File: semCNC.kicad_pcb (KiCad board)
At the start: 2 copper layers, 134 parts, among them P1 CONN_01X04, P10 CONN_01X05, P11 CONN_01X03, P12 CONN_02X08, P13 CONN_01X05, P14 CONN_01X03, P15 CONN_02X08, P16 CONN_01X05, P17 CONN_01X03, P18 CONN_02X08, P19 POWER_HEAD, P2 LPT port, P3 CONN_01X04, P4 EXPANDER PAD, P5 CONN_01X02, P6 CONN_01X02, P7 CONN_01X05, P8 CONN_01X03, P9 CONN_02X08, T1 TRANSFO, U1 MSP430G2452, U2 TIdac08s085, U3 LD1117S33CTR, U4 SPX2920U-3.3, U5 DRV8825, U6 DRV8825, U7 DRV8825, U8 DRV8825

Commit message: mer elegem van .... :P
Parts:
- added P20: CONN_01X02, Pin_Headers:Pin_Header_Straight_1x02, F.Cu at (587.6, 98.4)
- C12, C7, C8, C9: moved to B.Cu
- moved R14 146.3 mm to (351.4, 95.4), turned to 180 degrees
- moved R9 141.1 mm to (367.4, 140.1)
- moved R5 134.7 mm to (367.4, 148.7)
- moved R10 134.4 mm to (367.4, 144.4), turned to 180 degrees
- moved R17 126.8 mm to (375.6, 176.1)
- moved P6 120.0 mm to (602.1, 114.9)
- moved R13 106.3 mm to (383.7, 157.1), turned to 180 degrees
- moved P19 104.6 mm to (529.5, 104.2), turned to 90 degrees
- moved R6 99.1 mm to (399.4, 89.7), turned to 90 degrees
- moved C5 83.1 mm to (560.5, 115.1), turned to 270 degrees
- moved C6 81.4 mm to (579.3, 114.8), turned to 270 degrees
- moved C3 78.1 mm to (462.2, 81.1)
- moved C4 69.4 mm to (447.7, 81.1)
- moved R11 69.2 mm to (457.1, 105.5)
- moved R3 63.5 mm to (521.9, 100.2)
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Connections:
- C14 pad 2: GND -> VMOT_GND
- C15 pad 1: GND -> VMOT_GND
- C19 pad 2: GND -> VMOT_GND
- C20 pad 1: GND -> VMOT_GND
- C24 pad 2: GND -> VMOT_GND
- C25 pad 1: GND -> VMOT_GND
- C29 pad 2: GND -> VMOT_GND
- C30 pad 1: GND -> VMOT_GND
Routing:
- net VMOT_GND: track 9.77 -> 507.7 mm, vias 2 -> 4
- net VMOT: track 226.2 -> 508.6 mm, vias 0 -> 2
- net Net-(P2-Pad2): track 95.4 -> 5.17 mm, vias 1 -> 0
- net 3.3V: track 669.4 -> 742.8 mm, vias 3 -> 4
- net GND: track 48.4 -> 87.9 mm
- net /DRIVER3/STEP: track 34.2 -> 57.9 mm
- net Net-(P5-Pad1): track 24.6 -> 42.4 mm
- net Net-(P5-Pad2): track 22.1 -> 39.0 mm
- net /DRIVER2/STEP: track 36.8 -> 52.1 mm
- net Net-(D1-Pad4): track 30.8 -> 16.9 mm
- net Net-(D1-Pad2): track 41.4 -> 27.5 mm
- net Net-(P3-Pad3): track 39.7 -> 45.6 mm, vias 0 -> 1
- net /MOSI: track 18.5 -> 24.0 mm, vias 0 -> 2
- net /DRIVER4/DIR: track 23.9 -> 28.6 mm
- net /DRIVER1/DIR: track 52.8 -> 57.4 mm
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
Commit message: kicsit tovabb
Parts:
- moved R14 224.3 mm to (559.7, 178.7)
- moved R12 111.5 mm to (558.0, 170.0)
- moved R11 111.5 mm to (544.2, 175.1)
- moved C1 97.0 mm to (497.2, 175.9)
- moved C3 97.0 mm to (497.2, 171.6)
- moved R6 73.3 mm to (428.4, 157.1)
- moved P19 73.1 mm to (524.6, 177.1)
- moved R15 73.1 mm to (517.3, 182.0)
- moved R16 73.1 mm to (525.9, 182.0)
- moved R3 73.1 mm to (517.1, 173.1)
- moved R4 73.1 mm to (525.7, 173.1)
- moved C7 47.5 mm to (591.4, 101.7)
- moved C5 41.9 mm to (601.4, 106.0), turned to 180 degrees
- moved P20 36.8 mm to (591.4, 135.0)
- moved C6 22.9 mm to (601.2, 121.5), turned to 180 degrees
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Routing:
- net 3.3V: track 742.8 -> 649.1 mm
- net /DRIVER4/STEP: track 25.1 -> 67.5 mm, vias 1 -> 2
- net /DRIVER4/nFAULT: track 32.2 -> 70.3 mm, vias 1 -> 2
- net /DRIVER4/DIR: track 28.6 -> 66.5 mm, vias 1 -> 2
- net /DRIVER4/CURR_REF: track 47.5 -> 83.2 mm, vias 0 -> 1
- net VMOT: track 508.6 -> 541.9 mm, vias 2 -> 4
- net /DRIVER1/CURR_REF: track 74.8 -> 45.4 mm
- net /DRIVER3/CURR_REF: track 71.6 -> 45.1 mm
- net /DRIVER2/CURR_REF: track 78.8 -> 56.3 mm
- net /DRIVER1/DIR: track 57.4 -> 35.6 mm
- net /DRIVER3/nFAULT: track 61.1 -> 39.5 mm
- net /DRIVER1/nFAULT: track 77.7 -> 56.7 mm
- net /DRIVER3/DIR: track 44.0 -> 29.2 mm
- net /DRIVER2/nFAULT: track 56.5 -> 42.4 mm
- net /DRIVER1/STEP: track 57.6 -> 45.2 mm
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
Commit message: New layout
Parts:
- added P21: CONN_01X02, Pin_Headers:Pin_Header_Straight_1x02, F.Cu at (386.0, 159.4)
- R1, R10, R11, R12, R13, R14, R15, R16, R2, R3, R4, R5, R6, R7, R8, R9: moved to B.Cu
- moved P18 309.4 mm to (603.6, 194.2), turned to 180 degrees
- moved RV4 272.7 mm to (579.5, 199.3), turned to 0 degrees
- moved D5 271.9 mm to (587.1, 185.3), turned to 270 degrees
- moved R57 257.2 mm to (580.4, 182.3), turned to 0 degrees
- moved R59 254.9 mm to (580.4, 179.7), turned to 0 degrees
- moved R58 252.8 mm to (580.4, 177.2), turned to 180 degrees
- moved P17 252.6 mm to (569.1, 196.8), turned to 0 degrees
- moved R60 250.7 mm to (580.4, 174.7), turned to 0 degrees
- moved R61 248.4 mm to (580.4, 171.8), turned to 0 degrees
- moved R62 246.2 mm to (580.4, 168.7), turned to 0 degrees
- moved R63 244.4 mm to (580.4, 166.2), turned to 0 degrees
- moved R64 242.7 mm to (580.4, 163.6), turned to 0 degrees
- moved R65 241.1 mm to (580.4, 161.1), turned to 0 degrees
- moved C32 230.0 mm to (566.8, 179.0), turned to 180 degrees
- moved P16 228.4 mm to (552.8, 198.0), turned to 180 degrees
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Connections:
- P2 pad 11: /DRIVER2/nFAULT -> /DRIVER3/nFAULT
- P2 pad 12: /DRIVER3/nFAULT -> /DRIVER2/nFAULT
- P2 pad 18: GND -> Net-(P2-Pad18)
- P2 pad 19: GND -> Net-(P2-Pad18)
- P2 pad 20: GND -> Net-(P2-Pad18)
- P2 pad 21: GND -> Net-(P2-Pad18)
- P2 pad 22: GND -> Net-(P2-Pad18)
- P2 pad 23: GND -> Net-(P2-Pad18)
- P2 pad 24: GND -> Net-(P2-Pad18)
- P2 pad 25: GND -> Net-(P2-Pad18)
- R10 pad 1: /DRIVER3/STEP -> /DRIVER2/STEP
- R11 pad 2: /DRIVER3/DIR -> /DRIVER2/DIR
- R12 pad 1: /DRIVER3/DIR -> /DRIVER2/DIR
- R5 pad 2: /DRIVER2/STEP -> /DRIVER3/STEP
- R6 pad 1: /DRIVER2/STEP -> /DRIVER3/STEP
- R7 pad 2: /DRIVER2/DIR -> /DRIVER3/DIR
- R8 pad 1: /DRIVER2/DIR -> /DRIVER3/DIR
- R9 pad 2: /DRIVER3/STEP -> /DRIVER2/STEP
- U1 pad 11: /DRIVER4/STEP -> /DRIVER1/STEP
- U1 pad 15: /DRIVER1/STEP -> /DRIVER4/STEP
- U2 pad 3: /DRIVER3/CURR_REF -> /DRIVER2/CURR_REF
- U2 pad 4: /DRIVER2/CURR_REF -> /DRIVER3/CURR_REF
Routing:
- net 3.3V: track 649.1 -> 961.2 mm, vias 4 -> 2
- net /DRIVER1/DIR: track 35.6 -> 220.0 mm, vias 1 -> 3
- net /DRIVER1/STEP: track 45.2 -> 222.2 mm, vias 1 -> 3
- net /DRIVER4/STEP: track 67.5 -> 239.6 mm, vias 2 -> 3
- net /DRIVER4/DIR: track 66.5 -> 223.5 mm, vias 2 -> 3
- net /DRIVER4/CURR_REF: track 83.2 -> 239.4 mm
- net /DRIVER1/CURR_REF: track 45.4 -> 198.4 mm, vias 0 -> 1
- net /DRIVER2/STEP: track 43.9 -> 190.6 mm, vias 1 -> 3
- net /DRIVER2/DIR: track 35.7 -> 181.3 mm, vias 1 -> 3
- net /DRIVER3/DIR: track 29.2 -> 158.3 mm, vias 1 -> 3
- net /DRIVER2/CURR_REF: track 56.3 -> 180.3 mm, vias 0 -> 1
- net /DRIVER3/CURR_REF: track 45.1 -> 160.4 mm, vias 0 -> 1
- net /DRIVER3/STEP: track 50.5 -> 162.0 mm, vias 1 -> 3
- net /DRIVER2/nFAULT: track 42.4 -> 92.7 mm
- net /DRIVER3/nFAULT: track 39.5 -> 76.5 mm
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
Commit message: new layout
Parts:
- R21, R22, R23, R24, R25, R26, R27, R28, R29, R45, R46, R47, R48, R49, R50, R51, R52, R53, R57, R58, R59, R60, R61, R62, R63, R64, R65: moved to B.Cu
- moved P15 161.2 mm to (625.0, 95.3), turned to 90 degrees
- moved R45 149.9 mm to (632.5, 75.0), turned to 0 degrees
- moved R50 149.9 mm to (632.5, 90.0), turned to 0 degrees
- moved R47 149.9 mm to (632.5, 77.5), turned to 0 degrees
- moved R51 149.9 mm to (632.5, 92.5), turned to 0 degrees
- moved R46 149.9 mm to (632.5, 80.0), turned to 180 degrees
- moved R52 149.9 mm to (632.5, 95.0), turned to 0 degrees
- moved R48 149.8 mm to (632.5, 82.5), turned to 0 degrees
- moved R53 149.8 mm to (632.5, 97.5), turned to 0 degrees
- moved R49 149.8 mm to (632.5, 85.0), turned to 0 degrees
- moved P6 148.1 mm to (475.2, 57.8), turned to 180 degrees
- moved D4 134.7 mm to (632.5, 67.8), turned to 270 degrees
- moved P16 134.4 mm to (649.8, 105.0), turned to 0 degrees
- moved U7 131.8 mm to (632.2, 89.5)
- moved C27 131.5 mm to (635.0, 77.5)
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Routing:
- net 3.3V: track 961.2 -> 695.0 mm, vias 2 -> 1
- net /DRIVER4/CURR_REF: track 239.4 -> 18.6 mm, vias 1 -> 0
- net /DRIVER4/DIR: track 223.5 -> 5.94 mm, vias 3 -> 1
- net /DRIVER1/CURR_REF: track 198.4 -> 0.00 mm, vias 1 -> 0
- net /DRIVER4/STEP: track 239.6 -> 41.2 mm, vias 3 -> 1
- net /DRIVER1/DIR: track 220.0 -> 28.3 mm, vias 3 -> 1
- net /DRIVER1/STEP: track 222.2 -> 37.7 mm, vias 3 -> 1
- net /DRIVER3/CURR_REF: track 160.4 -> 16.6 mm, vias 1 -> 0
- net VMOT: track 525.7 -> 390.5 mm, vias 4 -> 2
- net /DRIVER3/DIR: track 158.3 -> 26.2 mm, vias 3 -> 1
- net /DRIVER2/CURR_REF: track 180.3 -> 52.4 mm, vias 1 -> 0
- net /DRIVER3/STEP: track 162.0 -> 37.0 mm, vias 3 -> 1
- net /DRIVER2/STEP: track 190.6 -> 76.7 mm
- net /DRIVER2/DIR: track 181.3 -> 67.5 mm
- net VMOT_GND: track 471.9 -> 362.9 mm, vias 4 -> 2
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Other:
- net class Default: clearance 0.254 -> 0.3048; via_dia 1 -> 1.6; via_drill 0.4 -> 0.8
- rule trace_clearance: 0.254 -> 0.3048
- board text added: "A rács 0.25mm-es, de csak a nagyobbakat használod ( hátra zoom ) A drv8825 közepe egy nagy rácspontra kerül, mellé a mikrokapcsoló, szimmetrikusan, a legfelső lábát rácspontra helyezve. 1206-os alkatrészeket mindig középen megfogva kell használni, mindig rácspontra kerül. Viák mindig rácspontra kerülnek, kivéve a kettőt, azok a felére. A mikrokapcsolót a 15-ös lábnál kell megfogni, az kerül rácsp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"

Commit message: layout work
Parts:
- R33, R34, R35, R36, R37, R38, R39, R40, R41: moved to B.Cu
- moved C4 237.3 mm to (691.8, 53.5), turned to 270 degrees
- moved P11 183.3 mm to (650.0, 95.2), turned to 180 degrees
- moved RV2 181.2 mm to (655.0, 93.0), turned to 180 degrees
- moved P10 181.0 mm to (627.7, 92.8), turned to 0 degrees
- moved P12 173.7 mm to (652.5, 67.5), turned to 270 degrees
- moved C19 171.1 mm to (632.5, 85.2), turned to 0 degrees
- moved R31 170.5 mm to (625.0, 75.2)
- moved R32 170.2 mm to (625.0, 80.2)
- moved R30 169.6 mm to (640.0, 65.2), turned to 180 degrees
- moved C20 169.2 mm to (632.5, 67.8), turned to 180 degrees
- moved C21 168.7 mm to (640.0, 70.2)
- moved U6 167.9 mm to (645.3, 73.2)
- moved C22 167.8 mm to (643.2, 85.5)
- moved C18 166.4 mm to (640.0, 67.8), turned to 0 degrees
- moved D3 163.1 mm to (645.0, 92.7)
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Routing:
- net (no net): track 17.4 -> 328.3 mm
- net VMOT: track 390.5 -> 107.5 mm, vias 2 -> 0
- net VMOT_GND: track 362.9 -> 88.6 mm, vias 2 -> 0
- net 3.3V: track 695.0 -> 507.6 mm
- net /DRIVER2/nHOME: track 67.3 -> 0.00 mm, vias 1 -> 0
- net /DRIVER2/MODE2: track 60.7 -> 0.00 mm, vias 1 -> 0
- net /DRIVER2/AOUT1: track 55.7 -> 0.00 mm, vias 1 -> 0
- net /DRIVER2/DIR: track 67.5 -> 14.2 mm, vias 3 -> 1
- net /DRIVER2/CURR_REF: track 52.4 -> 2.11 mm
- net /DRIVER2/MODE1: track 50.1 -> 0.00 mm, vias 1 -> 0
- net /DRIVER2/MODE0: track 45.1 -> 0.00 mm, vias 1 -> 0
- net /DRIVER2/AOUT2: track 45.1 -> 0.00 mm, vias 1 -> 0
- net /DRIVER2/STEP: track 76.7 -> 35.1 mm, vias 3 -> 1
- net Net-(P2-Pad18): track 40.7 -> 0.00 mm
- net /DRIVER2/nFAULT: track 39.9 -> 0.00 mm, vias 1 -> 0
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
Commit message: minor changes in layout
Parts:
- removed C3: C, Capacitors_SMD:C_1206_HandSoldering
- U2: value TIdac08s085 -> ANALOG_DEVICES_AD7304; footprint libs:TI_VSSOP10_DGS -> Housings_SOIC:SOIC-16_7.5x10.3mm_Pitch1.27mm
- moved P10 176.1 mm to (792.3, 30.5), turned to 180 degrees
- moved R32 174.0 mm to (795.0, 43.0), turned to 0 degrees
- moved R31 172.2 mm to (795.0, 48.0), turned to 0 degrees
- moved C19 162.0 mm to (787.5, 38.0), turned to 180 degrees
- moved C4 160.1 mm to (531.8, 45.5), turned to 0 degrees
- moved C20 155.5 mm to (787.5, 55.5), turned to 0 degrees
- moved P4 148.7 mm to (645.0, 107.3), turned to 0 degrees
- moved D3 144.1 mm to (775.0, 30.5), turned to 90 degrees
- moved C22 141.8 mm to (776.8, 37.8), turned to 0 degrees
- moved C21 141.1 mm to (780.0, 53.0), turned to 0 degrees
- moved C18 140.5 mm to (780.0, 55.5), turned to 180 degrees
- moved R30 140.2 mm to (780.0, 58.0), turned to 0 degrees
- moved R33 140.1 mm to (775.0, 35.5), turned to 0 degrees
- moved R35 138.3 mm to (775.0, 38.0), turned to 0 degrees
- moved P11 137.6 mm to (770.0, 28.0), turned to 0 degrees
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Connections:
- C1 pad 1: 3.3V -> GND
- C1 pad 2: GND -> 3.3V
- P10 pad 5: Net-(P10-Pad5) -> (no net)
- P13 pad 5: Net-(P13-Pad5) -> (no net)
- P16 pad 5: Net-(P16-Pad5) -> (no net)
- P7 pad 5: Net-(P7-Pad5) -> (no net)
- U1 pad 5: Net-(U1-Pad5) -> (no net)
- U2 pad 1: 3.3V -> /DRIVER1/CURR_REF
- U2 pad 2: /DRIVER4/CURR_REF -> /DRIVER3/CURR_REF
- U2 pad 3: /DRIVER2/CURR_REF -> (no net)
- U2 pad 4: /DRIVER3/CURR_REF -> 3.3V
- U2 pad 5: /DRIVER1/CURR_REF -> 3.3V
- U2 pad 7: 3.3V -> GND
- U2 pad 8: /MOSI -> 3.3V
- U5 pad 23: Net-(U5-Pad23) -> (no net)
- U6 pad 23: Net-(U6-Pad23) -> (no net)
- U7 pad 23: Net-(U7-Pad23) -> (no net)
- U8 pad 23: Net-(U8-Pad23) -> (no net)
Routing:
- net (no net): track 328.3 -> 122.1 mm
- net 3.3V: track 507.6 -> 613.2 mm
- net VMOT: track 107.5 -> 157.6 mm
- net VMOT_GND: track 88.6 -> 127.4 mm
- net /DRIVER3/AOUT1: track 0.00 -> 37.0 mm, vias 0 -> 1
- net Net-(P2-Pad18): track 0.00 -> 32.3 mm
- net Net-(P14-Pad2): track 0.00 -> 30.9 mm, vias 0 -> 2
- net /DRIVER3/CURR_REF: track 1.54 -> 32.2 mm
- net /PIN11: track 0.00 -> 27.9 mm
- net Net-(P8-Pad2): track 2.69 -> 30.2 mm, vias 0 -> 2
- net /DRIVER3/AOUT2: track 0.00 -> 26.2 mm, vias 0 -> 1
- net /PIN10: track 0.00 -> 25.3 mm
- net GND: track 58.1 -> 82.6 mm
- net /PIN9: track 0.00 -> 21.7 mm
- net /DRIVER3/BOUT2: track 0.00 -> 19.9 mm, vias 0 -> 1
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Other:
- net class Default: clearance 0.3048 -> 0.2286; via_dia 1.6 -> 1.4; via_drill 0.8 -> 0.5
- rule trace_clearance: 0.3048 -> 0.2286

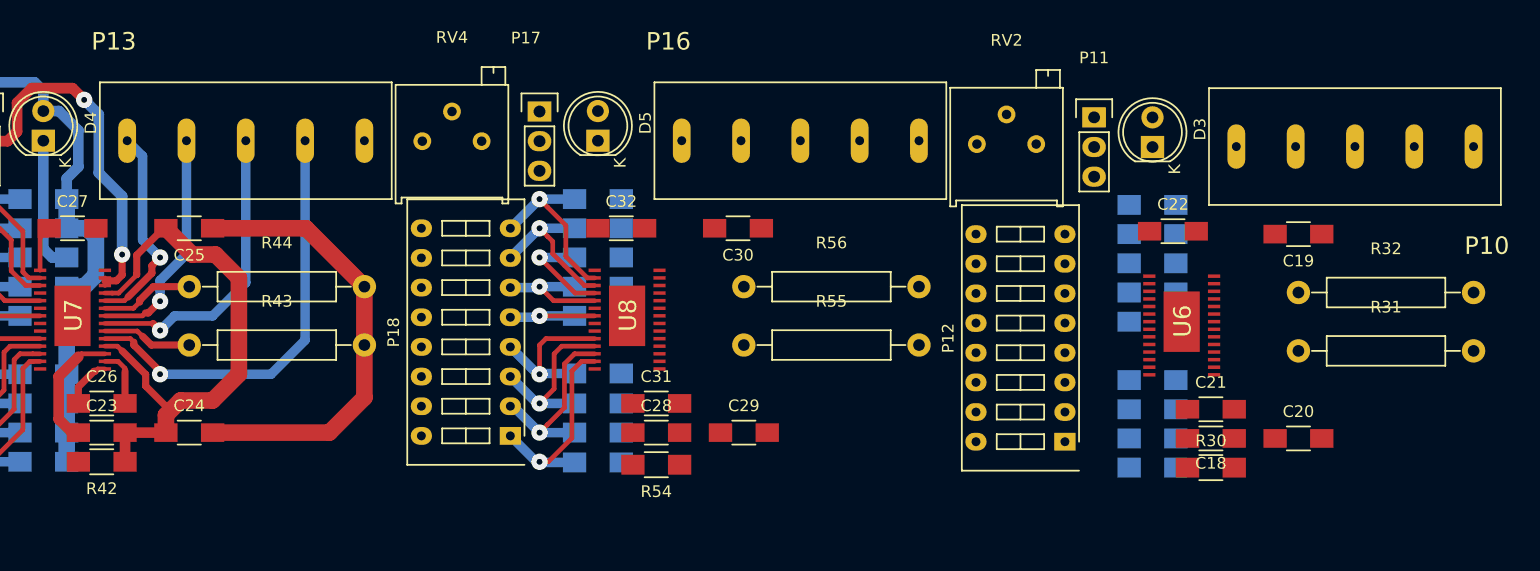
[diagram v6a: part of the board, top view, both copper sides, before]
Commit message: layout of drivers ready
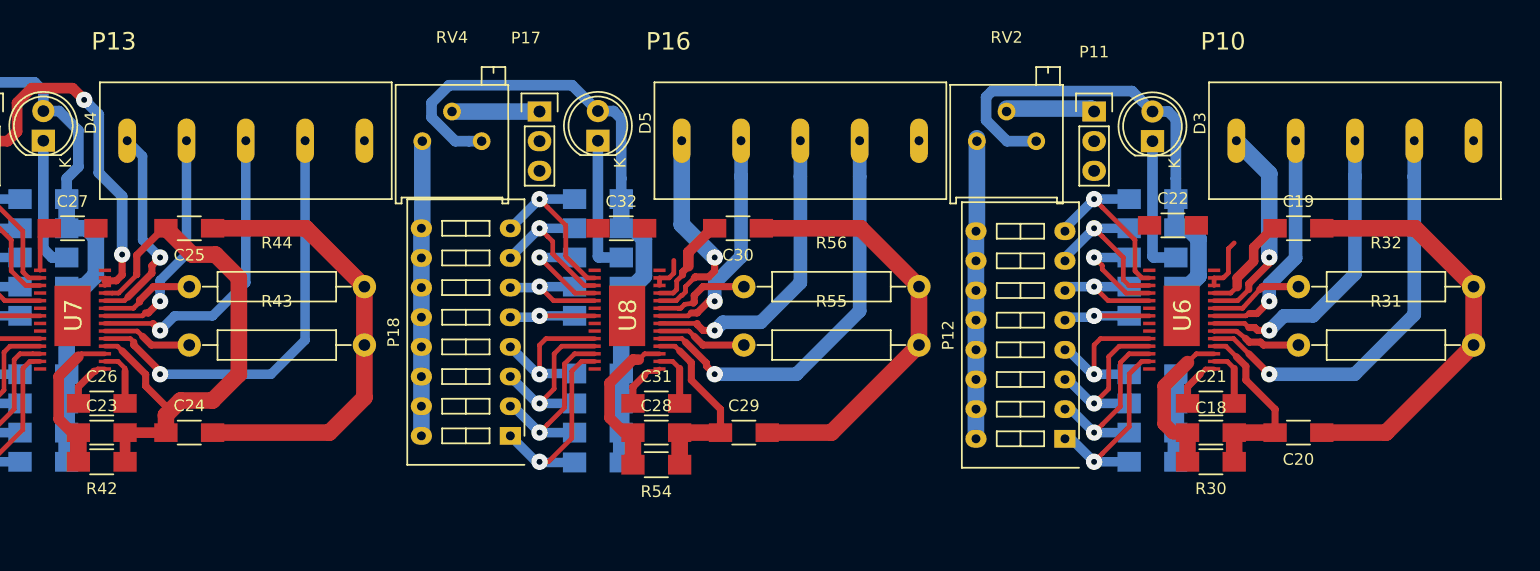
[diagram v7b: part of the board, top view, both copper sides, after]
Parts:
- moved C18 0.50 mm to (780.0, 55.0), turned to 0 degrees
- moved C19 0.50 mm to (787.5, 37.5), turned to 0 degrees
- moved C20 0.50 mm to (787.5, 55.0), turned to 180 degrees
- moved C21 0.50 mm to (780.0, 52.5)
- moved C22 0.50 mm to (776.8, 37.2)
- moved D3 0.50 mm to (775.0, 30.0)
- moved P10 0.50 mm to (792.3, 30.0), turned to 0 degrees
- moved P11 0.50 mm to (770.0, 27.5)
- moved R30 0.50 mm to (780.0, 57.5), turned to 180 degrees
- moved R31 0.50 mm to (795.0, 47.5)
- moved R32 0.50 mm to (795.0, 42.5)
- moved R33 0.50 mm to (775.0, 35.0)
- moved R34 0.50 mm to (775.0, 40.0)
- moved R35 0.50 mm to (775.0, 37.5)
- moved R36 0.50 mm to (775.0, 42.5)
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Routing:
- net 3.3V: track 613.2 -> 721.6 mm
- net VMOT_GND: track 127.4 -> 200.2 mm
- net GND: track 82.6 -> 133.3 mm
- net VMOT: track 157.6 -> 207.3 mm
- net /DRIVER2/AOUT1: track 0.00 -> 35.4 mm, vias 0 -> 1
- net /DRIVER4/AOUT1: track 0.00 -> 35.4 mm, vias 0 -> 1
- net /DRIVER4/AOUT2: track 0.00 -> 26.2 mm, vias 0 -> 1
- net /DRIVER2/AOUT2: track 0.00 -> 25.7 mm, vias 0 -> 1
- net /DRIVER4/BOUT2: track 0.00 -> 19.9 mm, vias 0 -> 1
- net /DRIVER2/BOUT2: track 0.00 -> 19.9 mm, vias 0 -> 1
- net /DRIVER4/BOUT1: track 0.00 -> 18.4 mm, vias 0 -> 1
- net /DRIVER2/BOUT1: track 0.00 -> 18.0 mm, vias 0 -> 1
- net /DRIVER2/nHOME: track 0.00 -> 17.3 mm, vias 0 -> 1
- net /DRIVER2/MODE2: track 0.00 -> 16.2 mm, vias 0 -> 1
- net /DRIVER2/nRESET: track 0.00 -> 15.6 mm, vias 0 -> 1
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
